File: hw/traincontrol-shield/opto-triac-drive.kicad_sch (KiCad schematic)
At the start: 6 parts, among them U5 MOC3021M, U6 MOC3021M

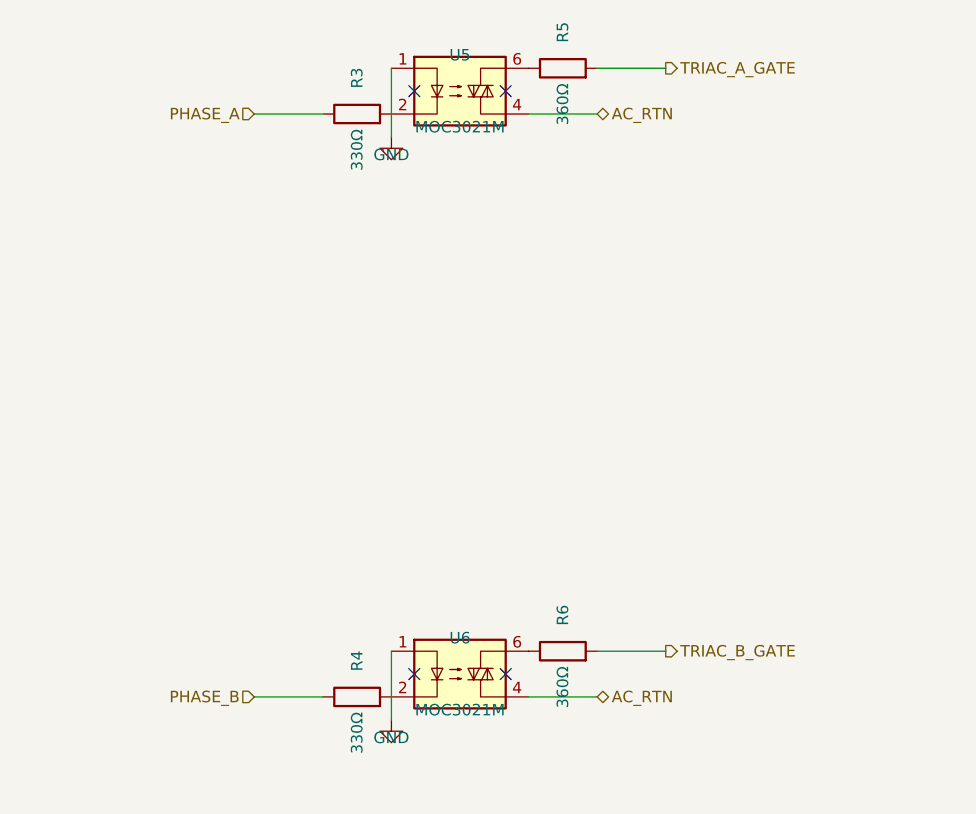
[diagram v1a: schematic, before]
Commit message: Increase component spacing to eliminate pin-wire overlaps
- zero-crossing: move R1 left 7.62mm, add bridge wire to U2 pin2
- xor-interlock: move C10 right of U3 output (76→91mm), move C11 right (168→178mm)
- opto-triac: add 7.62mm COMP_GAP between MOC3021 and LED/gate resistors
- triacs-snubbers: move snubber column right (99→109mm), add 7.62mm gap between R and C
- mcu: widen C4/C5/C6 decap spacing from 7.62mm to 10.16mm
- power-supply: move R13 down 7.62mm, add bridge wire to R12

Co-Authored-By: Claude Sonnet 4.6 <noreply@anthropic.com>
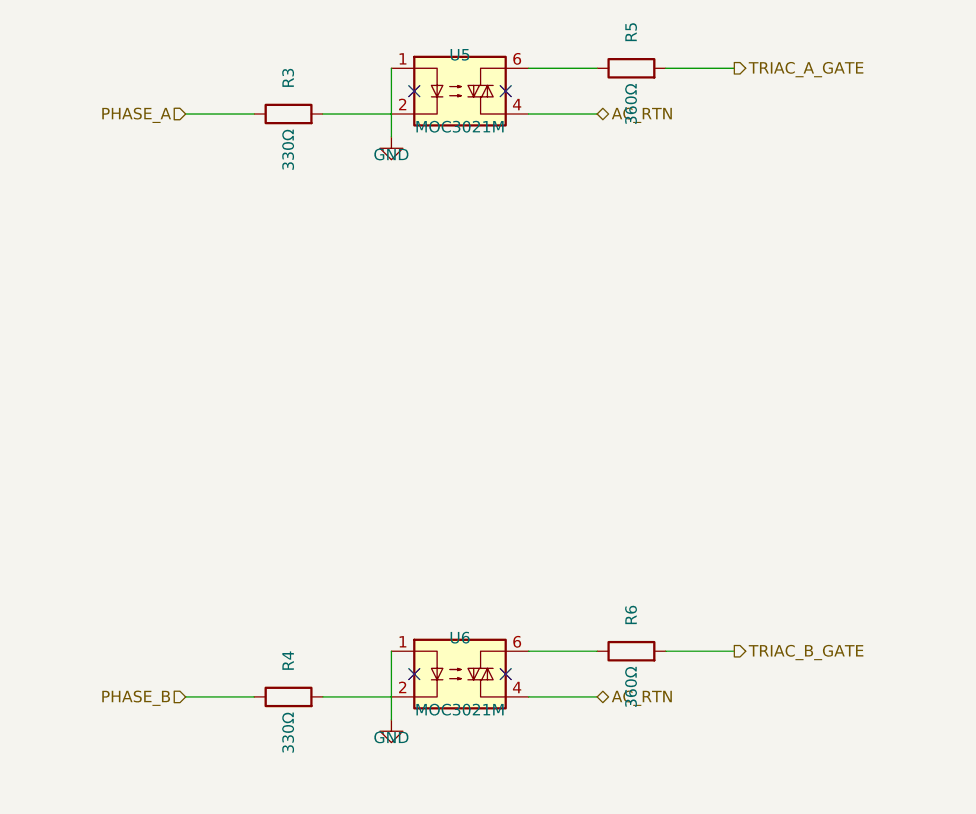
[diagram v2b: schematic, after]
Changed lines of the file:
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@@
 	(symbol
 		(lib_id "Device:R")
-		(at 68.58 92.71000000000001 90)
+		(at 60.959999999999994 92.71000000000001 90)
 		(unit 1)
 		(exclude_from_sim no)
@@
 		(dnp no)
 		(property "Reference" "R3"
-			(at 68.58 88.71000000000001 0)
+			(at 60.959999999999994 88.71000000000001 0)
 			(effects (font (size 1.27 1.27)))
 		)
 		(property "Value" "330Ω"
-			(at 68.58 96.71000000000001 0)
+			(at 60.959999999999994 96.71000000000001 0)
 			(effects (font (size 1.27 1.27)))
 		)
 		(property "Footprint" "Resistor_SMD:R_0603_1608Metric"
-			(at 68.58 92.71000000000001 0)
-			(effects (font (size 1.27 1.27)) (hide yes))
-		)
-		(property "Datasheet" "~"
-			(at 68.58 92.71000000000001 0)
+			(at 60.959999999999994 92.71000000000001 0)
+			(effects (font (size 1.27 1.27)) (hide yes))
+		)
+		(property "Datasheet" "~"
+			(at 60.959999999999994 92.71000000000001 0)
 			(effects (font (size 1.27 1.27)) (hide yes))
 		)
@@
 	)
 	(wire
-		(pts (xy 57.15 92.71000000000001) (xy 64.77 92.71000000000001))
+		(pts (xy 64.77 92.71000000000001) (xy 72.39 92.71000000000001))
+		(stroke (width 0) (type solid))
+	)
+	(wire
+		(pts (xy 49.529999999999994 92.71000000000001) (xy 57.14999999999999 92.71000000000001))
 		(stroke (width 0) (type solid))
 	)
 	(hierarchical_label "PHASE_A"
 		(shape input)
-		(at 57.15 92.71000000000001 180)
+		(at 49.529999999999994 92.71000000000001 180)
 		(fields_autoplaced yes)
 		(effects (font (size 1.27 1.27)) (justify right bottom))
 		(property "Intersheetrefs" "${INTERSHEET_REFS}"
-			(at 57.15 92.71000000000001 0)
+			(at 49.529999999999994 92.71000000000001 0)
 			(effects (font (size 1.27 1.27)) (hide yes))
 		)
@@
 	(symbol
 		(lib_id "Device:R")
-		(at 91.44000000000001 87.63 90)
+		(at 99.06000000000002 87.63 90)
 		(unit 1)
 		(exclude_from_sim no)
@@
 		(dnp no)
 		(property "Reference" "R5"
-			(at 91.44000000000001 83.63 0)
+			(at 99.06000000000002 83.63 0)
 			(effects (font (size 1.27 1.27)))
 		)
 		(property "Value" "360Ω"
-			(at 91.44000000000001 91.63 0)
+			(at 99.06000000000002 91.63 0)
 			(effects (font (size 1.27 1.27)))
 		)
 		(property "Footprint" "Resistor_SMD:R_0603_1608Metric"
-			(at 91.44000000000001 87.63 0)
-			(effects (font (size 1.27 1.27)) (hide yes))
-		)
-		(property "Datasheet" "~"
-			(at 91.44000000000001 87.63 0)
+			(at 99.06000000000002 87.63 0)
+			(effects (font (size 1.27 1.27)) (hide yes))
+		)
+		(property "Datasheet" "~"
+			(at 99.06000000000002 87.63 0)
 			(effects (font (size 1.27 1.27)) (hide yes))
 		)
@@
 	)
 	(wire
-		(pts (xy 87.63000000000001 87.63) (xy 87.63000000000001 87.63))
-		(stroke (width 0) (type solid))
-	)
-	(wire
-		(pts (xy 95.25000000000001 87.63) (xy 102.87000000000002 87.63))
+		(pts (xy 87.63000000000001 87.63) (xy 95.25000000000001 87.63))
+		(stroke (width 0) (type solid))
+	)
+	(wire
+		(pts (xy 102.87000000000002 87.63) (xy 110.49000000000002 87.63))
 		(stroke (width 0) (type solid))
 	)
 	(hierarchical_label "TRIAC_A_GATE"
 		(shape output)
-		(at 102.87000000000002 87.63 0)
+		(at 110.49000000000002 87.63 0)
 		(fields_autoplaced yes)
 		(effects (font (size 1.27 1.27)) (justify left bottom))
 		(property "Intersheetrefs" "${INTERSHEET_REFS}"
-			(at 102.87000000000002 87.63 0)
+			(at 110.49000000000002 87.63 0)
 			(effects (font (size 1.27 1.27)) (hide yes))
 		)
@@
 	(symbol
 		(lib_id "Device:R")
-		(at 68.58 157.48 90)
+		(at 60.959999999999994 157.48 90)
 		(unit 1)
 		(exclude_from_sim no)
@@
 		(dnp no)
 		(property "Reference" "R4"
-			(at 68.58 153.48 0)
+			(at 60.959999999999994 153.48 0)
 			(effects (font (size 1.27 1.27)))
 		)
 		(property "Value" "330Ω"
-			(at 68.58 161.48 0)
+			(at 60.959999999999994 161.48 0)
 			(effects (font (size 1.27 1.27)))
 		)
 		(property "Footprint" "Resistor_SMD:R_0603_1608Metric"
-			(at 68.58 157.48 0)
-			(effects (font (size 1.27 1.27)) (hide yes))
-		)
-		(property "Datasheet" "~"
-			(at 68.58 157.48 0)
+			(at 60.959999999999994 157.48 0)
+			(effects (font (size 1.27 1.27)) (hide yes))
+		)
+		(property "Datasheet" "~"
+			(at 60.959999999999994 157.48 0)
 			(effects (font (size 1.27 1.27)) (hide yes))
 		)
@@
 	)
 	(wire
-		(pts (xy 57.15 157.48) (xy 64.77 157.48))
+		(pts (xy 64.77 157.48) (xy 72.39 157.48))
+		(stroke (width 0) (type solid))
+	)
+	(wire
+		(pts (xy 49.529999999999994 157.48) (xy 57.14999999999999 157.48))
 		(stroke (width 0) (type solid))
 	)
 	(hierarchical_label "PHASE_B"
 		(shape input)
-		(at 57.15 157.48 180)
+		(at 49.529999999999994 157.48 180)
 		(fields_autoplaced yes)
 		(effects (font (size 1.27 1.27)) (justify right bottom))
 		(property "Intersheetrefs" "${INTERSHEET_REFS}"
-			(at 57.15 157.48 0)
+			(at 49.529999999999994 157.48 0)
 			(effects (font (size 1.27 1.27)) (hide yes))
 		)
@@
 	(symbol
 		(lib_id "Device:R")
-		(at 91.44000000000001 152.4 90)
+		(at 99.06000000000002 152.4 90)
 		(unit 1)
 		(exclude_from_sim no)
@@
 		(dnp no)
 		(property "Reference" "R6"
-			(at 91.44000000000001 148.4 0)
+			(at 99.06000000000002 148.4 0)
 			(effects (font (size 1.27 1.27)))
 		)
 		(property "Value" "360Ω"
-			(at 91.44000000000001 156.4 0)
+			(at 99.06000000000002 156.4 0)
 			(effects (font (size 1.27 1.27)))
 		)
 		(property "Footprint" "Resistor_SMD:R_0603_1608Metric"
-			(at 91.44000000000001 152.4 0)
-			(effects (font (size 1.27 1.27)) (hide yes))
-		)
-		(property "Datasheet" "~"
-			(at 91.44000000000001 152.4 0)
+			(at 99.06000000000002 152.4 0)
+			(effects (font (size 1.27 1.27)) (hide yes))
+		)
+		(property "Datasheet" "~"
+			(at 99.06000000000002 152.4 0)
 			(effects (font (size 1.27 1.27)) (hide yes))
 		)
@@
 	)
 	(wire
-		(pts (xy 87.63000000000001 152.4) (xy 87.63000000000001 152.4))
-		(stroke (width 0) (type solid))
-	)
-	(wire
-		(pts (xy 95.25000000000001 152.4) (xy 102.87000000000002 152.4))
+		(pts (xy 87.63000000000001 152.4) (xy 95.25000000000001 152.4))
+		(stroke (width 0) (type solid))
+	)
+	(wire
+		(pts (xy 102.87000000000002 152.4) (xy 110.49000000000002 152.4))
 		(stroke (width 0) (type solid))
 	)
 	(hierarchical_label "TRIAC_B_GATE"
 		(shape output)
-		(at 102.87000000000002 152.4 0)
+		(at 110.49000000000002 152.4 0)
 		(fields_autoplaced yes)
 		(effects (font (size 1.27 1.27)) (justify left bottom))
 		(property "Intersheetrefs" "${INTERSHEET_REFS}"
-			(at 102.87000000000002 152.4 0)
-			(effects (font (size 1.27 1.27)) (hide yes))
-		)
+			(at 110.49000000000002 152.4 0)
+			(effects (font (size 1.27 1.27)) (hide yes))
+		)

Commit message: Enforce IC-to-passive body gap ≥ 2×STUB across all sheets
Computed symbol body extents from KiCad library and applied:
  IC-to-IC gap  = 4×STUB = 30.48mm between body edges
  IC-to-passive = 2×STUB = 15.24mm between body edges

Violations found and fixed:
- zero-crossing: R1 center 77.47→73.66mm (R1 body right→U2 body left = 15.24mm ✓)
- zero-crossing: R2 center 116.84→119.38mm (U2 body right→R2 body left = 16.76mm ✓)
- opto-triac: COMP_GAP 7.62→15.24mm (MOC body edge to R body edge = 19.05mm ✓)

All other spacings were already compliant (xor-interlock U3→U4 50.8mm,
triacs-snubbers TRIAC→R-sn 18mm, power-supply D1→C1 38mm).

Co-Authored-By: Claude Sonnet 4.6 <noreply@anthropic.com>
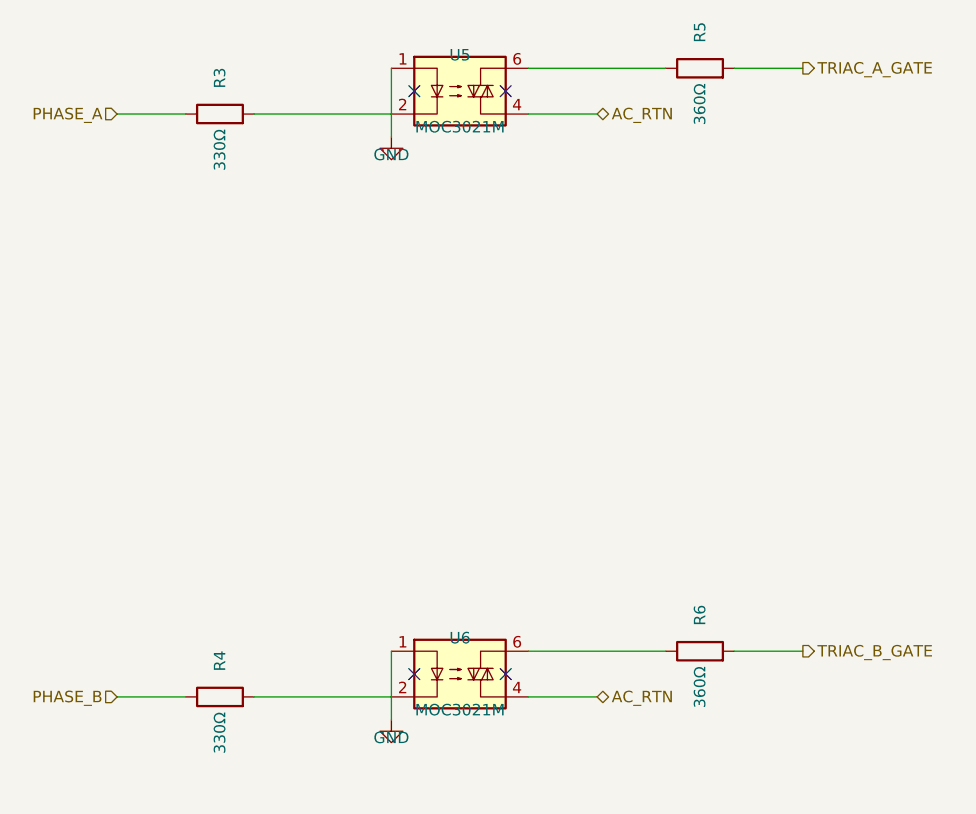
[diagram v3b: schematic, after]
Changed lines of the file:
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@@
 	(symbol
 		(lib_id "Device:R")
-		(at 60.959999999999994 92.71000000000001 90)
+		(at 53.339999999999996 92.71000000000001 90)
 		(unit 1)
 		(exclude_from_sim no)
@@
 		(dnp no)
 		(property "Reference" "R3"
-			(at 60.959999999999994 88.71000000000001 0)
+			(at 53.339999999999996 88.71000000000001 0)
 			(effects (font (size 1.27 1.27)))
 		)
 		(property "Value" "330Ω"
-			(at 60.959999999999994 96.71000000000001 0)
+			(at 53.339999999999996 96.71000000000001 0)
 			(effects (font (size 1.27 1.27)))
 		)
 		(property "Footprint" "Resistor_SMD:R_0603_1608Metric"
-			(at 60.959999999999994 92.71000000000001 0)
-			(effects (font (size 1.27 1.27)) (hide yes))
-		)
-		(property "Datasheet" "~"
-			(at 60.959999999999994 92.71000000000001 0)
+			(at 53.339999999999996 92.71000000000001 0)
+			(effects (font (size 1.27 1.27)) (hide yes))
+		)
+		(property "Datasheet" "~"
+			(at 53.339999999999996 92.71000000000001 0)
 			(effects (font (size 1.27 1.27)) (hide yes))
 		)
@@
 	)
 	(wire
-		(pts (xy 64.77 92.71000000000001) (xy 72.39 92.71000000000001))
-		(stroke (width 0) (type solid))
-	)
-	(wire
-		(pts (xy 49.529999999999994 92.71000000000001) (xy 57.14999999999999 92.71000000000001))
+		(pts (xy 57.15 92.71000000000001) (xy 72.39 92.71000000000001))
+		(stroke (width 0) (type solid))
+	)
+	(wire
+		(pts (xy 41.91 92.71000000000001) (xy 49.529999999999994 92.71000000000001))
 		(stroke (width 0) (type solid))
 	)
 	(hierarchical_label "PHASE_A"
 		(shape input)
-		(at 49.529999999999994 92.71000000000001 180)
+		(at 41.91 92.71000000000001 180)
 		(fields_autoplaced yes)
 		(effects (font (size 1.27 1.27)) (justify right bottom))
 		(property "Intersheetrefs" "${INTERSHEET_REFS}"
-			(at 49.529999999999994 92.71000000000001 0)
+			(at 41.91 92.71000000000001 0)
 			(effects (font (size 1.27 1.27)) (hide yes))
 		)
@@
 	(symbol
 		(lib_id "Device:R")
-		(at 99.06000000000002 87.63 90)
+		(at 106.68 87.63 90)
 		(unit 1)
 		(exclude_from_sim no)
@@
 		(dnp no)
 		(property "Reference" "R5"
-			(at 99.06000000000002 83.63 0)
+			(at 106.68 83.63 0)
 			(effects (font (size 1.27 1.27)))
 		)
 		(property "Value" "360Ω"
-			(at 99.06000000000002 91.63 0)
+			(at 106.68 91.63 0)
 			(effects (font (size 1.27 1.27)))
 		)
 		(property "Footprint" "Resistor_SMD:R_0603_1608Metric"
-			(at 99.06000000000002 87.63 0)
-			(effects (font (size 1.27 1.27)) (hide yes))
-		)
-		(property "Datasheet" "~"
-			(at 99.06000000000002 87.63 0)
+			(at 106.68 87.63 0)
+			(effects (font (size 1.27 1.27)) (hide yes))
+		)
+		(property "Datasheet" "~"
+			(at 106.68 87.63 0)
 			(effects (font (size 1.27 1.27)) (hide yes))
 		)
@@
 	)
 	(wire
-		(pts (xy 87.63000000000001 87.63) (xy 95.25000000000001 87.63))
-		(stroke (width 0) (type solid))
-	)
-	(wire
-		(pts (xy 102.87000000000002 87.63) (xy 110.49000000000002 87.63))
+		(pts (xy 87.63000000000001 87.63) (xy 102.87 87.63))
+		(stroke (width 0) (type solid))
+	)
+	(wire
+		(pts (xy 110.49000000000001 87.63) (xy 118.11000000000001 87.63))
 		(stroke (width 0) (type solid))
 	)
 	(hierarchical_label "TRIAC_A_GATE"
 		(shape output)
-		(at 110.49000000000002 87.63 0)
+		(at 118.11000000000001 87.63 0)
 		(fields_autoplaced yes)
 		(effects (font (size 1.27 1.27)) (justify left bottom))
 		(property "Intersheetrefs" "${INTERSHEET_REFS}"
-			(at 110.49000000000002 87.63 0)
+			(at 118.11000000000001 87.63 0)
 			(effects (font (size 1.27 1.27)) (hide yes))
 		)
@@
 	(symbol
 		(lib_id "Device:R")
-		(at 60.959999999999994 157.48 90)
+		(at 53.339999999999996 157.48 90)
 		(unit 1)
 		(exclude_from_sim no)
@@
 		(dnp no)
 		(property "Reference" "R4"
-			(at 60.959999999999994 153.48 0)
+			(at 53.339999999999996 153.48 0)
 			(effects (font (size 1.27 1.27)))
 		)
 		(property "Value" "330Ω"
-			(at 60.959999999999994 161.48 0)
+			(at 53.339999999999996 161.48 0)
 			(effects (font (size 1.27 1.27)))
 		)
 		(property "Footprint" "Resistor_SMD:R_0603_1608Metric"
-			(at 60.959999999999994 157.48 0)
-			(effects (font (size 1.27 1.27)) (hide yes))
-		)
-		(property "Datasheet" "~"
-			(at 60.959999999999994 157.48 0)
+			(at 53.339999999999996 157.48 0)
+			(effects (font (size 1.27 1.27)) (hide yes))
+		)
+		(property "Datasheet" "~"
+			(at 53.339999999999996 157.48 0)
 			(effects (font (size 1.27 1.27)) (hide yes))
 		)
@@
 	)
 	(wire
-		(pts (xy 64.77 157.48) (xy 72.39 157.48))
-		(stroke (width 0) (type solid))
-	)
-	(wire
-		(pts (xy 49.529999999999994 157.48) (xy 57.14999999999999 157.48))
+		(pts (xy 57.15 157.48) (xy 72.39 157.48))
+		(stroke (width 0) (type solid))
+	)
+	(wire
+		(pts (xy 41.91 157.48) (xy 49.529999999999994 157.48))
 		(stroke (width 0) (type solid))
 	)
 	(hierarchical_label "PHASE_B"
 		(shape input)
-		(at 49.529999999999994 157.48 180)
+		(at 41.91 157.48 180)
 		(fields_autoplaced yes)
 		(effects (font (size 1.27 1.27)) (justify right bottom))
 		(property "Intersheetrefs" "${INTERSHEET_REFS}"
-			(at 49.529999999999994 157.48 0)
+			(at 41.91 157.48 0)
 			(effects (font (size 1.27 1.27)) (hide yes))
 		)
@@
 	(symbol
 		(lib_id "Device:R")
-		(at 99.06000000000002 152.4 90)
+		(at 106.68 152.4 90)
 		(unit 1)
 		(exclude_from_sim no)
@@
 		(dnp no)
 		(property "Reference" "R6"
-			(at 99.06000000000002 148.4 0)
+			(at 106.68 148.4 0)
 			(effects (font (size 1.27 1.27)))
 		)
 		(property "Value" "360Ω"
-			(at 99.06000000000002 156.4 0)
+			(at 106.68 156.4 0)
 			(effects (font (size 1.27 1.27)))
 		)
 		(property "Footprint" "Resistor_SMD:R_0603_1608Metric"
-			(at 99.06000000000002 152.4 0)
-			(effects (font (size 1.27 1.27)) (hide yes))
-		)
-		(property "Datasheet" "~"
-			(at 99.06000000000002 152.4 0)
+			(at 106.68 152.4 0)
+			(effects (font (size 1.27 1.27)) (hide yes))
+		)
+		(property "Datasheet" "~"
+			(at 106.68 152.4 0)
 			(effects (font (size 1.27 1.27)) (hide yes))
 		)
@@
 	)
 	(wire
-		(pts (xy 87.63000000000001 152.4) (xy 95.25000000000001 152.4))
-		(stroke (width 0) (type solid))
-	)
-	(wire
-		(pts (xy 102.87000000000002 152.4) (xy 110.49000000000002 152.4))
+		(pts (xy 87.63000000000001 152.4) (xy 102.87 152.4))
+		(stroke (width 0) (type solid))
+	)
+	(wire
+		(pts (xy 110.49000000000001 152.4) (xy 118.11000000000001 152.4))
 		(stroke (width 0) (type solid))
 	)
 	(hierarchical_label "TRIAC_B_GATE"
 		(shape output)
-		(at 110.49000000000002 152.4 0)
+		(at 118.11000000000001 152.4 0)
 		(fields_autoplaced yes)
 		(effects (font (size 1.27 1.27)) (justify left bottom))
 		(property "Intersheetrefs" "${INTERSHEET_REFS}"
-			(at 110.49000000000002 152.4 0)
-			(effects (font (size 1.27 1.27)) (hide yes))
-		)
+			(at 118.11000000000001 152.4 0)
+			(effects (font (size 1.27 1.27)) (hide yes))
+		)
